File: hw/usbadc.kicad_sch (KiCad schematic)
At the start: 3 parts, among them J4 JTAG

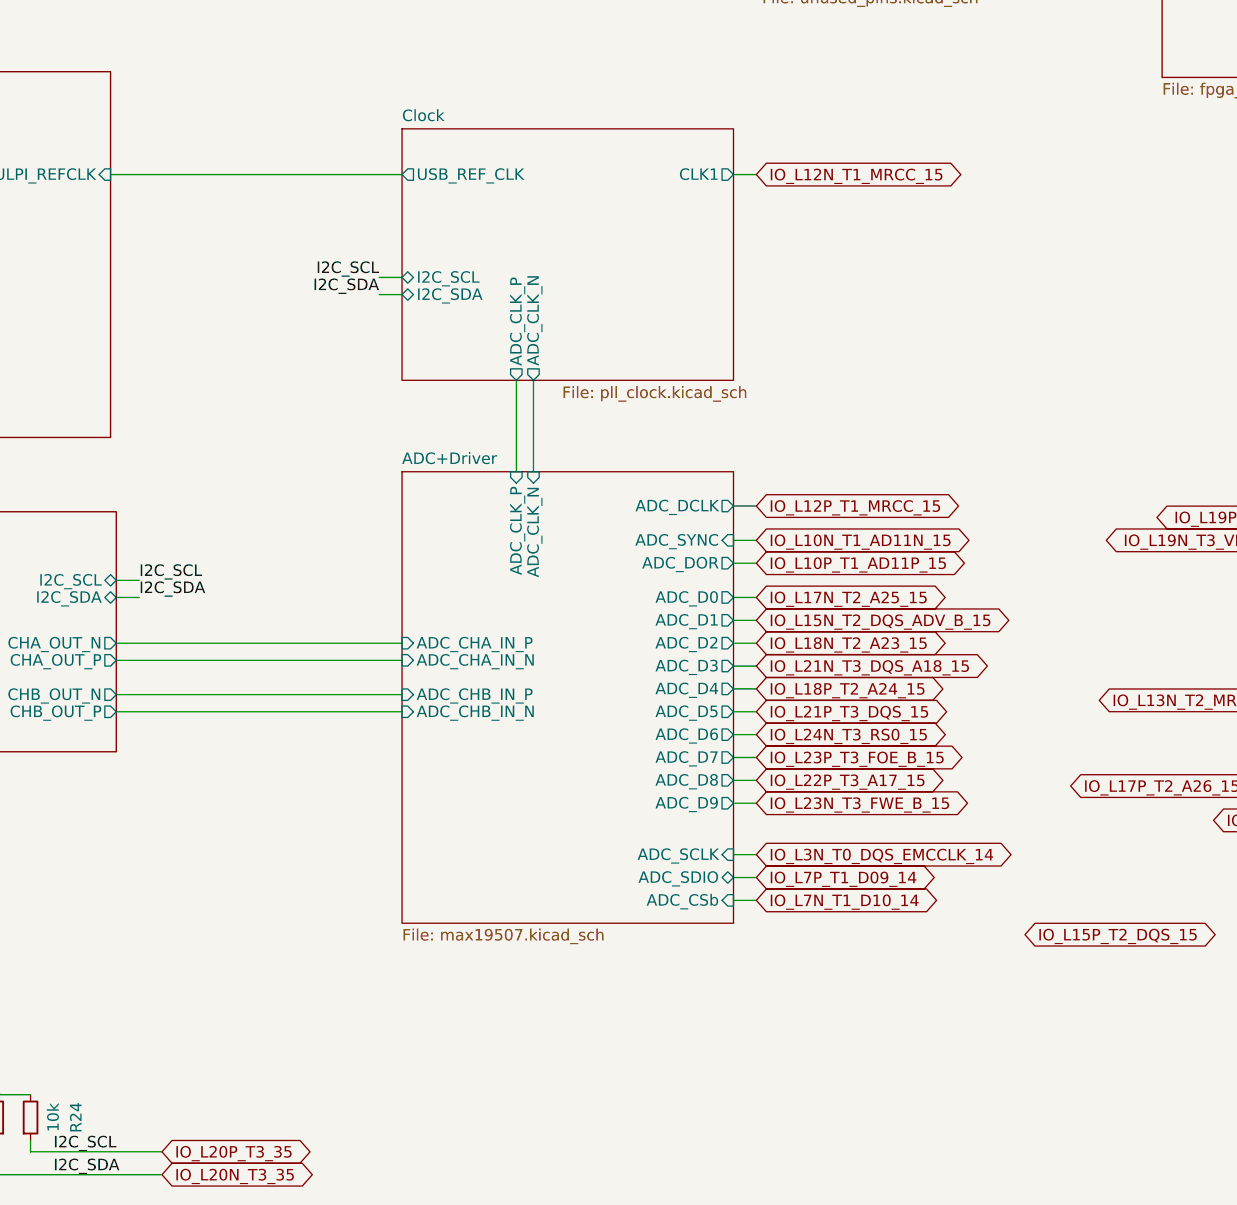
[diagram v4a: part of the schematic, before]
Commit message: WIP - almost everything except power (converters) connected
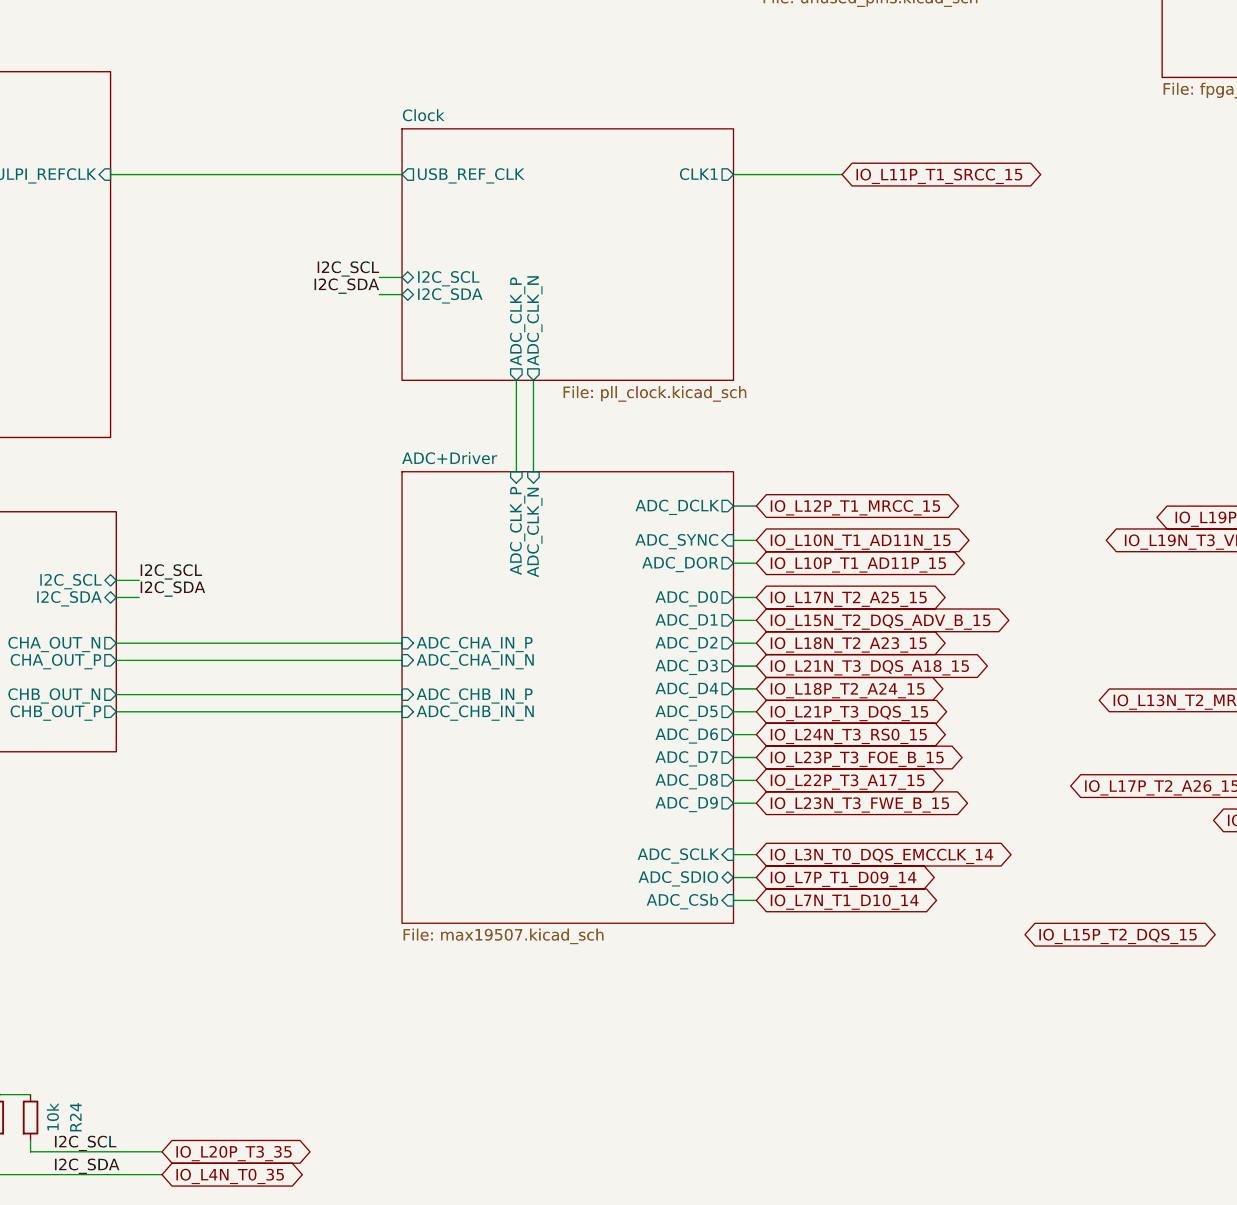
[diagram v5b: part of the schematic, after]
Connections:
- net IO_L20N_T3_35 renamed IO_L4N_T0_35
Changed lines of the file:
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@@
     (stroke (width 0) (type default))
   )
-  (wire (pts (xy 168.275 78.105) (xy 170.815 78.105))
+  (wire (pts (xy 168.275 78.105) (xy 180.34 78.105))
     (stroke (width 0) (type default))
   )
@@
     )
   )
-  (global_label "IO_L12N_T1_MRCC_15" (shape bidirectional) (at 170.815 78.105 0) (fields_autoplaced)
-    (effects (font (size 1.27 1.27)) (justify left))
-    (property "Intersheetrefs" "${INTERSHEET_REFS}" (at 194.4599 78.105 0)
+  (global_label "IO_L11P_T1_SRCC_15" (shape bidirectional) (at 180.34 78.105 0) (fields_autoplaced)
+    (effects (font (size 1.27 1.27)) (justify left))
+    (property "Intersheetrefs" "${INTERSHEET_REFS}" (at 203.6825 78.105 0)
       (effects (font (size 1.27 1.27)) (justify left) hide)
     )
@@
     )
   )
-  (global_label "IO_L20N_T3_35" (shape bidirectional) (at 104.775 189.23 0) (fields_autoplaced)
-    (effects (font (size 1.27 1.27)) (justify left))
-    (property "Intersheetrefs" "${INTERSHEET_REFS}" (at 122.1909 189.23 0)
-      (effects (font (size 1.27 1.27)) (justify left) hide)
-    )
+  (global_label "IO_L4N_T0_35" (shape bidirectional) (at 104.775 189.23 0) (fields_autoplaced)
+    (effects (font (size 1.27 1.27)) (justify left))
+    (property "Intersheetrefs" "${INTERSHEET_REFS}" (at 120.9814 189.23 0)
+      (effects (font (size 1.27 1.27)) (justify left) hide)
+    )

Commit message: layout finished (draft)
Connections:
- net IO_L20P_T3_35 renamed IO_L3P_T0_DQS_AD5P_35
- no-connect marks 1 -> 0
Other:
- sheet LEDs ports: added LED_CHA_B, LED_CHA_G, LED_CHA_R, LED_CHB_B, LED_CHB_G, LED_CHB_R; removed none
- sheet Power ports: added none; removed PG_2V5
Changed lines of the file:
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@@
   (junction (at 86.36 180.34) (diameter 0) (color 0 0 0 0)
   )
-  (no_connect (at 276.86 118.745))
   (wire (pts (xy 168.275 140.335) (xy 170.815 140.335))
     (stroke (width 0) (type default))
@@
     (stroke (width 0) (type default))
   )
+  (wire (pts (xy 255.905 92.075) (xy 259.08 92.075))
+    (stroke (width 0) (type default))
+  )
   (wire (pts (xy 168.275 121.285) (xy 170.815 121.285))
     (stroke (width 0) (type default))
@@
     (stroke (width 0) (type default))
   )
+  (wire (pts (xy 255.905 89.535) (xy 259.08 89.535))
+    (stroke (width 0) (type default))
+  )
+  (wire (pts (xy 255.905 80.01) (xy 259.08 80.01))
+    (stroke (width 0) (type default))
+  )
   (wire (pts (xy 131.445 89.535) (xy 128.905 89.535))
     (stroke (width 0) (type default))
@@
     (stroke (width 0) (type default))
   )
+  (wire (pts (xy 255.905 94.615) (xy 259.08 94.615))
+    (stroke (width 0) (type default))
+  )
   (wire (pts (xy 99.06 78.105) (xy 131.445 78.105))
     (stroke (width 0) (type default))
@@
     (stroke (width 0) (type default))
   )
-  (wire (pts (xy 274.955 118.745) (xy 276.86 118.745))
-    (stroke (width 0) (type default))
-  )
   (wire (pts (xy 168.275 127.635) (xy 170.815 127.635))
     (stroke (width 0) (type default))
@@
   )
   (wire (pts (xy 168.275 147.955) (xy 170.815 147.955))
+    (stroke (width 0) (type default))
+  )
+  (wire (pts (xy 255.905 85.09) (xy 259.08 85.09))
+    (stroke (width 0) (type default))
+  )
+  (wire (pts (xy 255.905 82.55) (xy 259.08 82.55))
     (stroke (width 0) (type default))
   )
@@
     )
   )
-  (global_label "IO_L22N_T3_A16_15" (shape bidirectional) (at 221.615 149.86 0) (fields_autoplaced)
-    (effects (font (size 1.27 1.27)) (justify left))
-    (property "Intersheetrefs" "${INTERSHEET_REFS}" (at 243.5061 149.86 0)
-      (effects (font (size 1.27 1.27)) (justify left) hide)
-    )
-  )
   (global_label "IO_L9N_T1_DQS_AD7N_35" (shape bidirectional) (at 50.165 99.06 180) (fields_autoplaced)
     (effects (font (size 1.27 1.27)) (justify right))
@@
     )
   )
+  (global_label "IO_L23N_T3_A02_D18_14" (shape bidirectional) (at 255.905 80.01 180) (fields_autoplaced)
+    (effects (font (size 1.27 1.27)) (justify right))
+    (property "Intersheetrefs" "${INTERSHEET_REFS}" (at 229.3573 80.01 0)
+      (effects (font (size 1.27 1.27)) (justify right) hide)
+    )
+  )
   (global_label "IO_L9P_T1_DQS_AD7P_35" (shape bidirectional) (at 50.165 96.52 180) (fields_autoplaced)
     (effects (font (size 1.27 1.27)) (justify right))
@@
     )
   )
+  (global_label "IO_L16N_T2_A15_D31_14" (shape bidirectional) (at 255.905 82.55 180) (fields_autoplaced)
+    (effects (font (size 1.27 1.27)) (justify right))
+    (property "Intersheetrefs" "${INTERSHEET_REFS}" (at 229.3573 82.55 0)
+      (effects (font (size 1.27 1.27)) (justify right) hide)
+    )
+  )
   (global_label "IO_L11P_T1_SRCC_15" (shape bidirectional) (at 180.34 78.105 0) (fields_autoplaced)
     (effects (font (size 1.27 1.27)) (justify left))
@@
     )
   )
+  (global_label "IO_L10N_T1_D15_14" (shape bidirectional) (at 255.905 85.09 180) (fields_autoplaced)
+    (effects (font (size 1.27 1.27)) (justify right))
+    (property "Intersheetrefs" "${INTERSHEET_REFS}" (at 233.8325 85.09 0)
+      (effects (font (size 1.27 1.27)) (justify right) hide)
+    )
+  )
   (global_label "IO_L10P_T1_AD15P_35" (shape bidirectional) (at 50.165 86.36 180) (fields_autoplaced)
     (effects (font (size 1.27 1.27)) (justify right))
@@
     )
   )
+  (global_label "IO_L9P_T1_DQS_14" (shape bidirectional) (at 255.905 89.535 180) (fields_autoplaced)
+    (effects (font (size 1.27 1.27)) (justify right))
+    (property "Intersheetrefs" "${INTERSHEET_REFS}" (at 234.9815 89.535 0)
+      (effects (font (size 1.27 1.27)) (justify right) hide)
+    )
+  )
   (global_label "IO_L19P_T3_35" (shape bidirectional) (at 231.775 116.205 180) (fields_autoplaced)
     (effects (font (size 1.27 1.27)) (justify right))
@@
     )
   )
+  (global_label "IO_L10P_T1_D14_14" (shape bidirectional) (at 255.905 92.075 180) (fields_autoplaced)
+    (effects (font (size 1.27 1.27)) (justify right))
+    (property "Intersheetrefs" "${INTERSHEET_REFS}" (at 233.893 92.075 0)
+      (effects (font (size 1.27 1.27)) (justify right) hide)
+    )
+  )
   (global_label "IO_L7N_T1_AD6N_35" (shape bidirectional) (at 50.165 93.98 180) (fields_autoplaced)
     (effects (font (size 1.27 1.27)) (justify right))
@@
     )
   )
-  (global_label "IO_L17P_T2_A26_15" (shape bidirectional) (at 205.74 146.05 0) (fields_autoplaced)
-    (effects (font (size 1.27 1.27)) (justify left))
-    (property "Intersheetrefs" "${INTERSHEET_REFS}" (at 227.5706 146.05 0)
-      (effects (font (size 1.27 1.27)) (justify left) hide)
-    )
-  )
   (global_label "IO_L22P_T3_A17_15" (shape bidirectional) (at 170.815 145.415 0) (fields_autoplaced)
     (effects (font (size 1.27 1.27)) (justify left))
@@
     )
   )
+  (global_label "IO_L16P_T2_CSI_B_14" (shape bidirectional) (at 255.905 94.615 180) (fields_autoplaced)
+    (effects (font (size 1.27 1.27)) (justify right))
+    (property "Intersheetrefs" "${INTERSHEET_REFS}" (at 232.2601 94.615 0)
+      (effects (font (size 1.27 1.27)) (justify right) hide)
+    )
+  )
   (global_label "IO_L8N_T1_D12_14" (shape bidirectional) (at 50.165 121.92 180) (fields_autoplaced)
     (effects (font (size 1.27 1.27)) (justify right))
@@
     )
   )
+  (global_label "IO_L3P_T0_DQS_AD5P_35" (shape bidirectional) (at 104.775 186.69 0) (fields_autoplaced)
+    (effects (font (size 1.27 1.27)) (justify left))
+    (property "Intersheetrefs" "${INTERSHEET_REFS}" (at 125.6985 186.69 0)
+      (effects (font (size 1.27 1.27)) (justify left) hide)
+    )
+  )
   (global_label "IO_L22P_T3_35" (shape bidirectional) (at 255.905 73.025 180) (fields_autoplaced)
     (effects (font (size 1.27 1.27)) (justify right))
@@
     )
   )
-  (global_label "IO_L13N_T2_MRCC_15" (shape bidirectional) (at 208.915 136.525 0) (fields_autoplaced)
-    (effects (font (size 1.27 1.27)) (justify left))
-    (property "Intersheetrefs" "${INTERSHEET_REFS}" (at 232.5599 136.525 0)
-      (effects (font (size 1.27 1.27)) (justify left) hide)
-    )
-  )
   (global_label "IO_L4P_T0_34" (shape bidirectional) (at 255.905 70.485 180) (fields_autoplaced)
     (effects (font (size 1.27 1.27)) (justify right))
@@
     )
   )
-  (global_label "IO_L15P_T2_DQS_15" (shape bidirectional) (at 200.66 162.56 0) (fields_autoplaced)
-    (effects (font (size 1.27 1.27)) (justify left))
-    (property "Intersheetrefs" "${INTERSHEET_REFS}" (at 222.793 162.56 0)
-      (effects (font (size 1.27 1.27)) (justify left) hide)
-    )
-  )
   (global_label "IO_L17P_T2_35" (shape bidirectional) (at 50.165 74.295 180) (fields_autoplaced)
     (effects (font (size 1.27 1.27)) (justify right))
@@
     (effects (font (size 1.27 1.27)) (justify left))
     (property "Intersheetrefs" "${INTERSHEET_REFS}" (at 192.6456 135.255 0)
-      (effects (font (size 1.27 1.27)) (justify left) hide)
-    )
-  )
-  (global_label "IO_L20P_T3_35" (shape bidirectional) (at 104.775 186.69 0) (fields_autoplaced)
-    (effects (font (size 1.27 1.27)) (justify left))
-    (property "Intersheetrefs" "${INTERSHEET_REFS}" (at 122.1304 186.69 0)
       (effects (font (size 1.27 1.27)) (justify left) hide)
     )
@@
       (effects (font (size 1.27 1.27)) (justify left))
     )
-    (pin "PG_2V5" output (at 274.955 118.745 0)
-      (effects (font (size 1.27 1.27)) (justify right))
-    )
     (instances
       (project "usbadc"
@@
       (effects (font (size 1.27 1.27)) (justify left))
     )
+    (pin "LED_CHB_B" input (at 259.08 94.615 180)
+      (effects (font (size 1.27 1.27)) (justify left))
+    )
+    (pin "LED_CHB_R" input (at 259.08 89.535 180)
+      (effects (font (size 1.27 1.27)) (justify left))
+    )
+    (pin "LED_CHB_G" input (at 259.08 92.075 180)
+      (effects (font (size 1.27 1.27)) (justify left))
+    )
+    (pin "LED_CHA_G" input (at 259.08 82.55 180)
+      (effects (font (size 1.27 1.27)) (justify left))
+    )
+    (pin "LED_CHA_B" input (at 259.08 85.09 180)
+      (effects (font (size 1.27 1.27)) (justify left))
+    )
+    (pin "LED_CHA_R" input (at 259.08 80.01 180)
+      (effects (font (size 1.27 1.27)) (justify left))
+    )

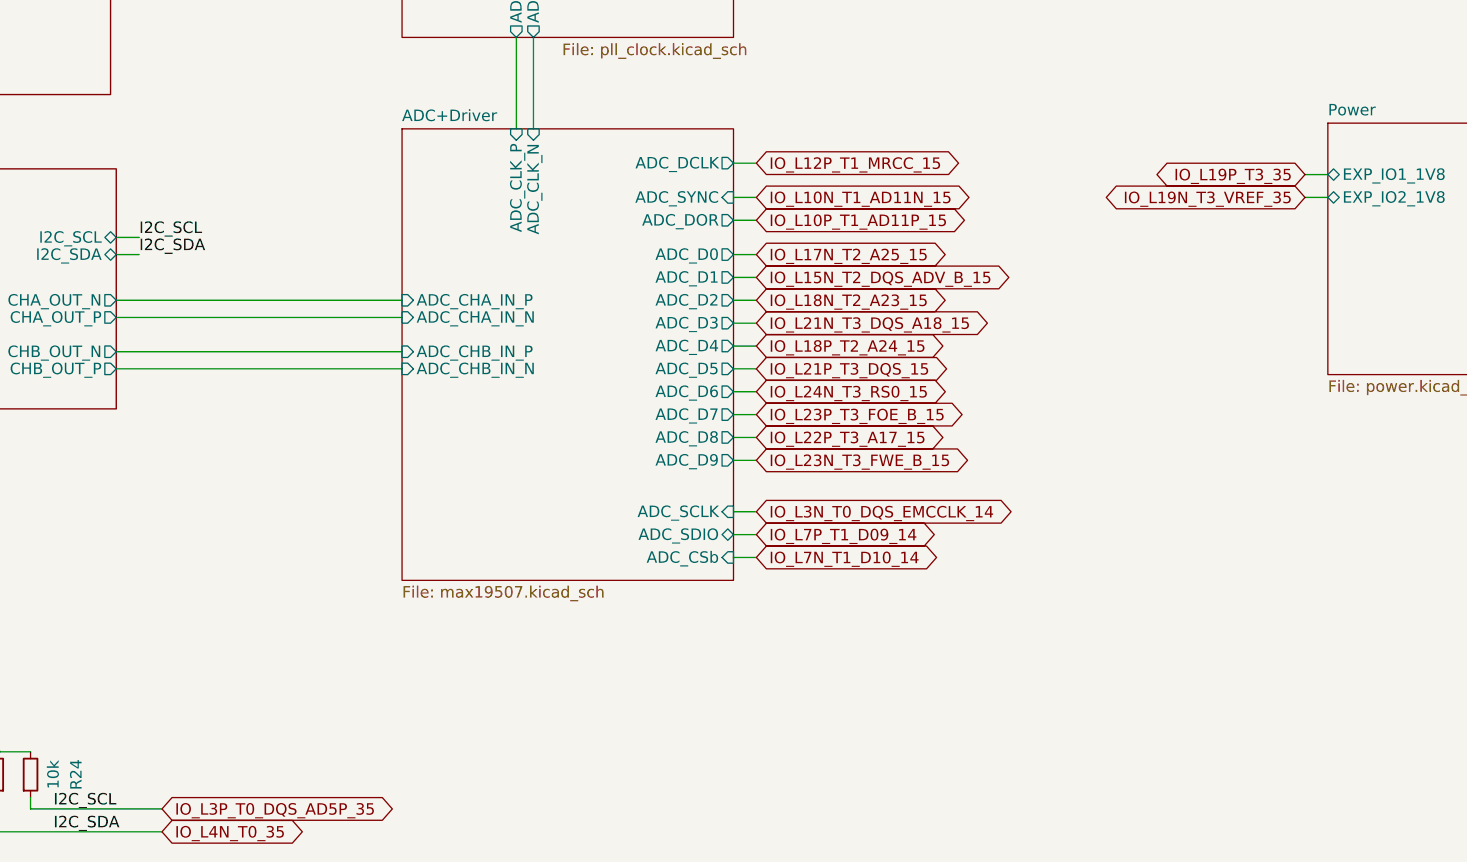
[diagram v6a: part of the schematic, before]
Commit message: finished routing; DRC passes (except for 1 hole violation at push-button)
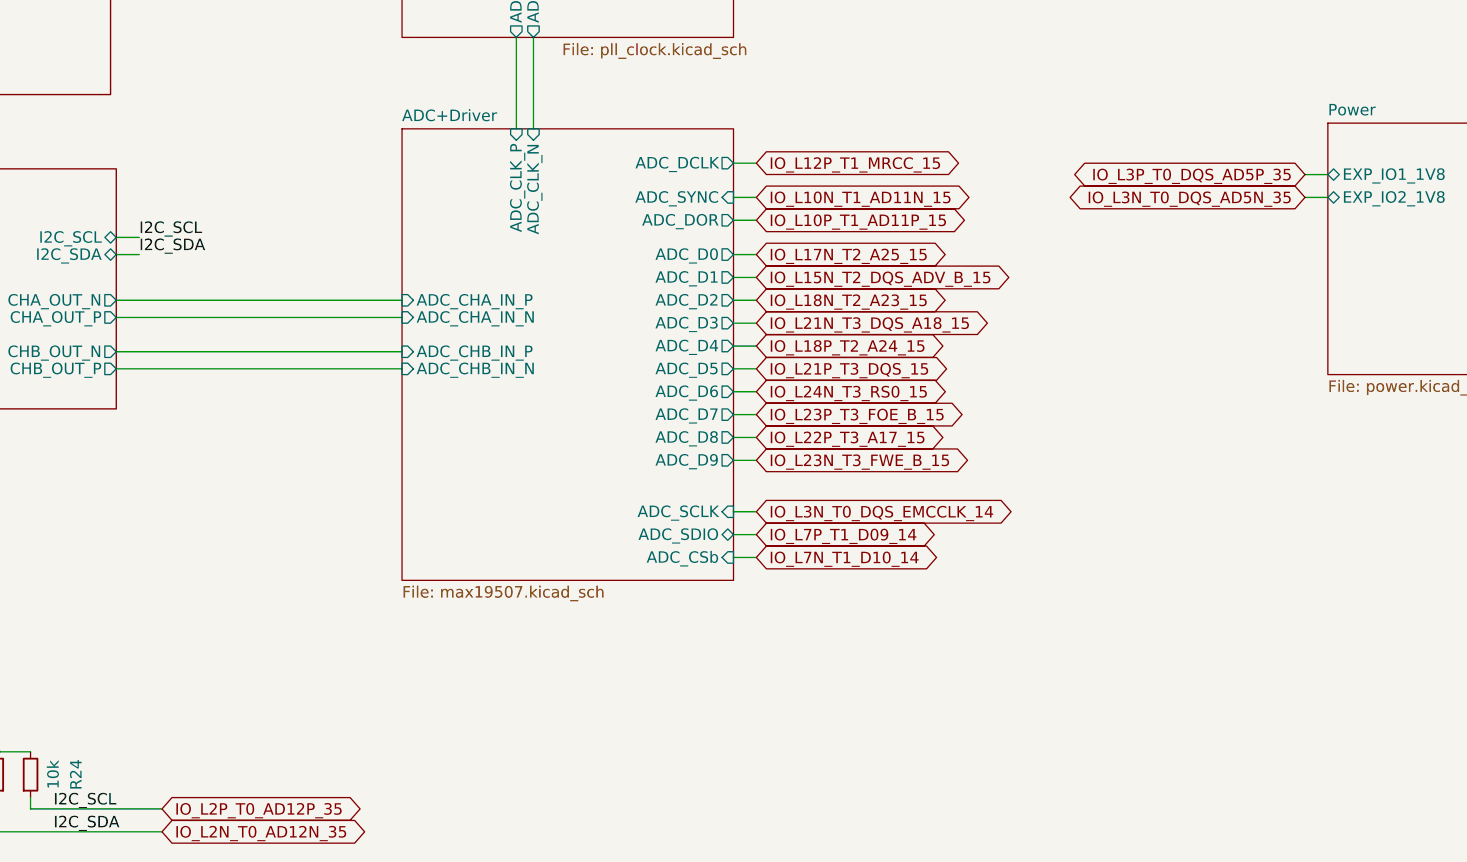
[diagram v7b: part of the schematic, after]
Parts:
- R23, R24: Manufacturer Yageo -> (none); Part RT0603FRE0710KL -> (none)
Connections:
- net IO_L3P_T0_DQS_AD5P_35: no longer R24.1
- net IO_L4N_T0_35 renamed IO_L2N_T0_AD12N_35
- new net IO_L2P_T0_AD12P_35: R24.1
